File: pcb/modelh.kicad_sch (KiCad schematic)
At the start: 46 parts, among them J1 Battery Conn, J2 Conn_01x20, J3 Conn_01x06, J4 Conn_01x12, J5 Conn_01x04, J6 Conn_01x04, SW1 SW_reset, U1 nice_nano, U2 74HC595, U3 74HC595, U4 74HC595

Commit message: 101 key was correct
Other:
- note added: "Keyboard Matrix - link"
- note added: "TE Connectivity Trio-mate connectors Can be replaced with Connfly FFC/FPC"
- note removed: "Keyboard Matrix"
- note removed: "TE Connectivity Trio-mate connectors"
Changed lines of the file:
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@@
 		)
 	)
-	(text "Keyboard Matrix"
+	(text "Keyboard Matrix - link"
 		(exclude_from_sim no)
-		(at 217.17 59.69 0)
+		(at 215.265 66.04 0)
 		(effects
 			(font
@@
 		)
 	)
-	(text "TE Connectivity Trio-mate connectors"
+	(text "TE Connectivity Trio-mate connectors\nCan be replaced with Connfly FFC/FPC"
 		(exclude_from_sim no)
-		(at 217.17 35.814 0)
+		(at 198.12 36.068 0)
 		(effects
 			(font
 				(size 1.27 1.27)
 			)
+			(justify left)
 		)
 	)
@@
 	)
 	(image
-		(at 215.646 47.498)
+		(at 215.773 55.626)
 		(scale 0.377794)
 		(data "iVBORw0KGgoAAAANSUhEUgAABAAAAAI7CAIAAAD9En6AAAAAA3NCSVQICAjb4U/gAAAgAElEQVR4"

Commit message: Mostly stylistic changes
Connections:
- net led0: now also U1.11 (011); no longer U1.13 (106)
- net led0r: now also R3.1; no longer R1.1
- net led2: now also U1.13 (106); no longer U1.11 (011)
- net led2r: now also R1.1; no longer R3.1
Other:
- moved on the sheet: R1, R3

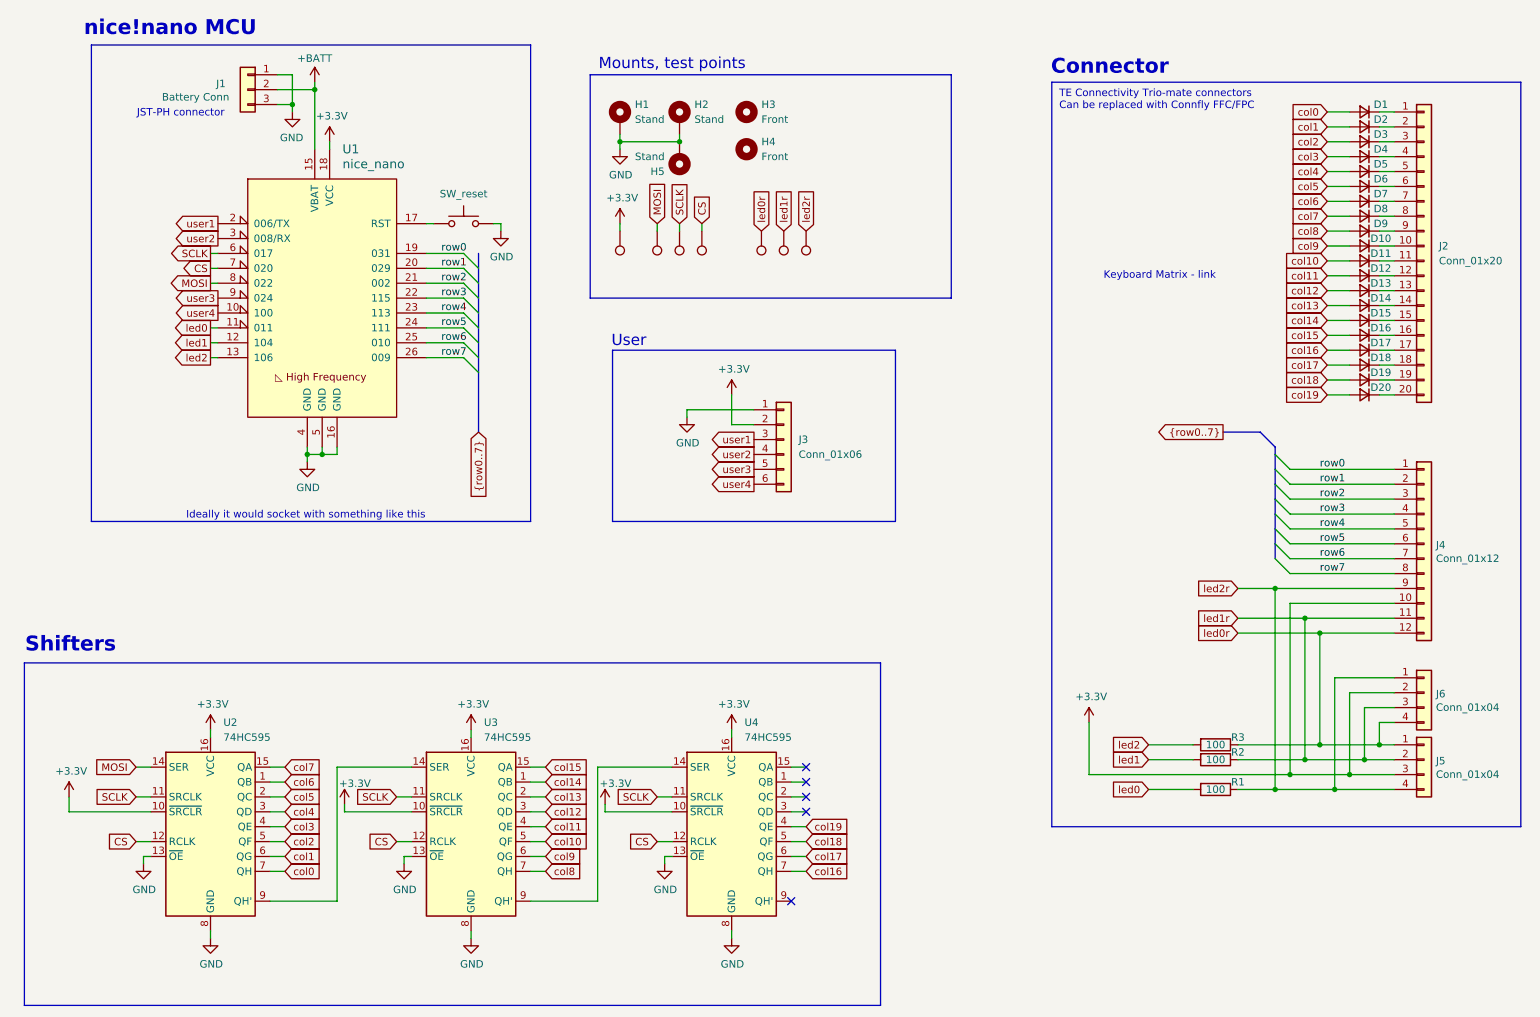
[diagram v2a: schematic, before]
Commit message: Better models, added SGA font, col0 separate
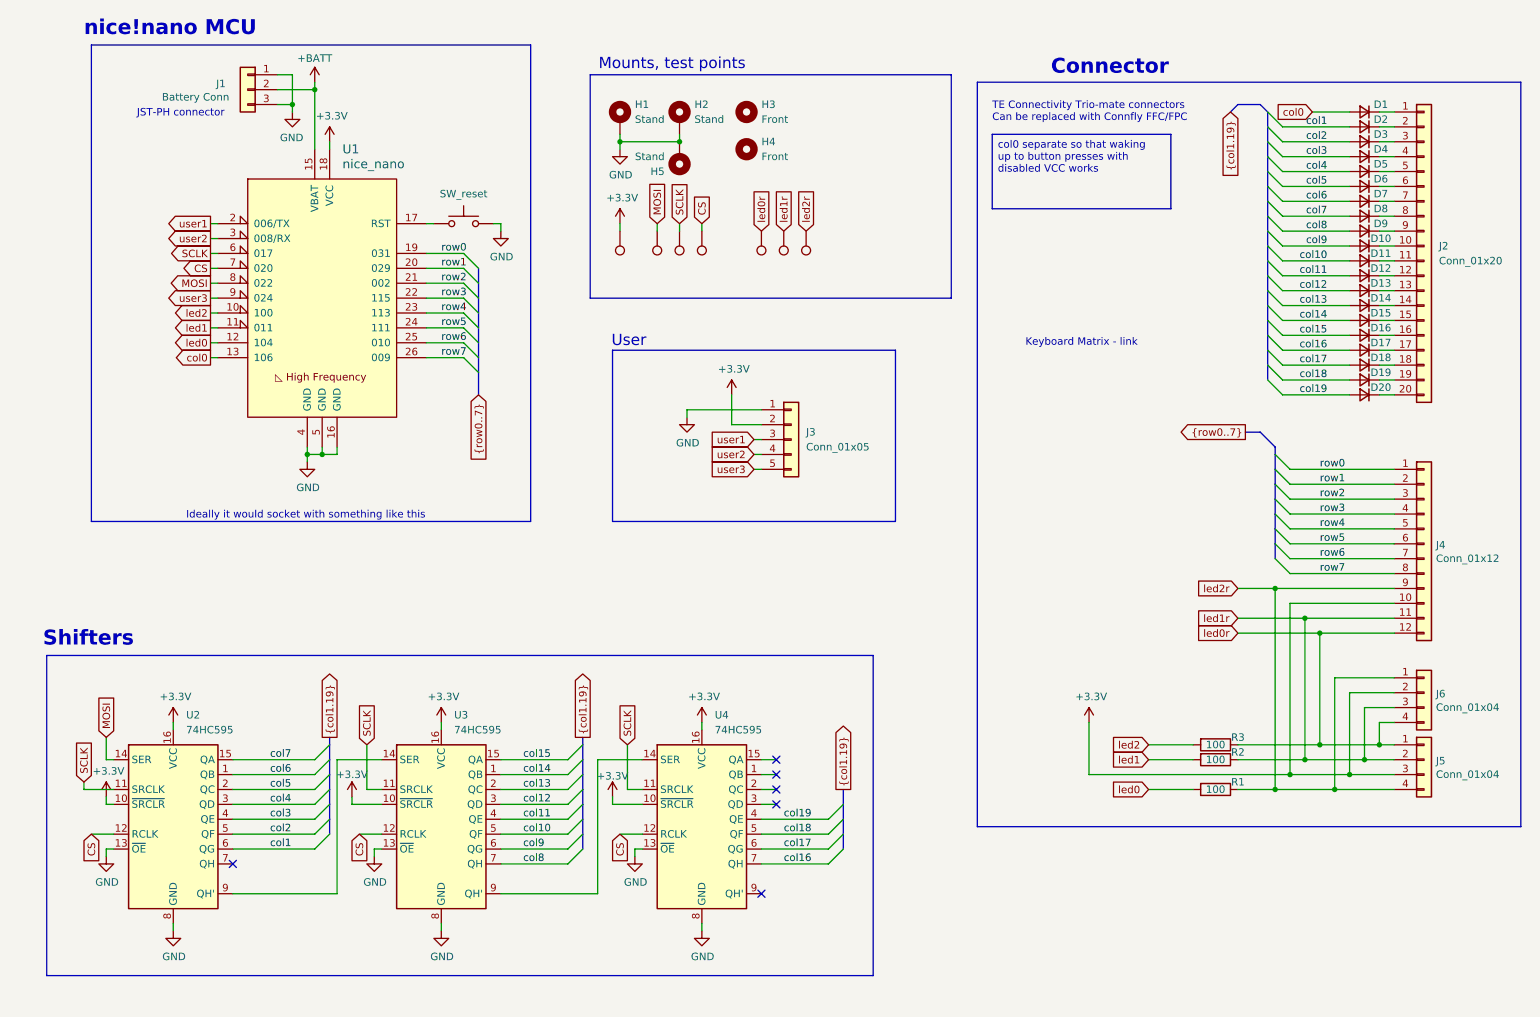
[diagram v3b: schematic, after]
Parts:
- removed J3: Conn_01x06, Connector_PinHeader_2.54mm:PinHeader_1x06_P2.54mm_Vertical, symbol Connector_Generic:Conn_01x06
- added J3: Conn_01x05, Connector_PinHeader_2.54mm:PinHeader_1x05_P2.54mm_Vertical, symbol Connector_Generic:Conn_01x05
- TP1: footprint Library:TestPoint -> TestPoint:TestPoint_Pad_D2.5mm
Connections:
- net user4 is gone; now on net led2: U1.10 (100)
- net +3.3V: now also J3.2 (Pin_2)
- net GND: now also J3.1 (Pin_1)
- net col0: now also U1.13 (106); no longer U2.7 (QH)
- net led0: now also U1.12 (104); no longer U1.11 (011)
- net led1: now also U1.11 (011); no longer U1.12 (104)
- net led2: no longer U1.13 (106)
- net user1: now also J3.3 (Pin_3)
- net user2: now also J3.4 (Pin_4)
- net user3: now also J3.5 (Pin_5)
- no-connect marks 5 -> 6
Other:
- moved on the sheet: U2, U3, U4

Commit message: v0.7, too much to comment
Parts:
- removed H5: Stand, MountingHole:MountingHole_4mm_Pad_Via, symbol Mechanical:MountingHole_Pad
- removed J6: Conn_01x04, Library:ModelH-triomate-leds4, symbol Connector_Generic:Conn_01x04
- removed TP1: VCC, TestPoint:TestPoint_Pad_D2.5mm, symbol Connector:TestPoint
- removed TP2: MOSI, Library:TestPoint, symbol Connector:TestPoint
- removed TP3: SCLK, Library:TestPoint, symbol Connector:TestPoint
- removed TP4: CS, Library:TestPoint, symbol Connector:TestPoint
- removed TP5: LED0, Library:TestPoint, symbol Connector:TestPoint
- removed TP6: LED1, Library:TestPoint, symbol Connector:TestPoint
- removed TP7: LED2, Library:TestPoint, symbol Connector:TestPoint
- added J6: Conn_01x08, Library:ModelH-triomate-rows8, symbol Connector_Generic:Conn_01x08
- R1, R2, R3: value 100 -> 150
- U2, U3, U4: footprint Package_DIP:DIP-16_W7.62mm_Socket_LongPads -> Library:DIP-16-74HC595
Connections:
- net CS: now also U1.6 (017); no longer U1.7 (020)
- net SCLK: now also U1.7 (020); no longer U1.6 (017)
- net row0: now also J6.1 (Pin_1)
- net row1: now also J6.2 (Pin_2)
- net row2: now also J6.3 (Pin_3)
- net row3: now also J6.4 (Pin_4)
- net row4: now also J6.5 (Pin_5)
- net row5: now also J6.6 (Pin_6)
- net row6: now also J6.7 (Pin_7)
- net row7: now also J6.8 (Pin_8)
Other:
- note added: "TE Connectivity Trio-mate connectors Can be replaced with Connfly FFC/FPC BUT rotated 180deg"
- note added: "This one is for the 122key one"
- note removed: "TE Connectivity Trio-mate connectors Can be replaced with Connfly FFC/FPC"
- moved on the sheet: D1, D10, D11, D12, D13, D14, D15, D16, D17, D18, D19, D2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
